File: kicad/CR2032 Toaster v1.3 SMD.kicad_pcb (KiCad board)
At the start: 2 copper layers, 26 x 16.5 mm, 8 parts, among them J1 Conn_01x01, J2 Conn_01x01

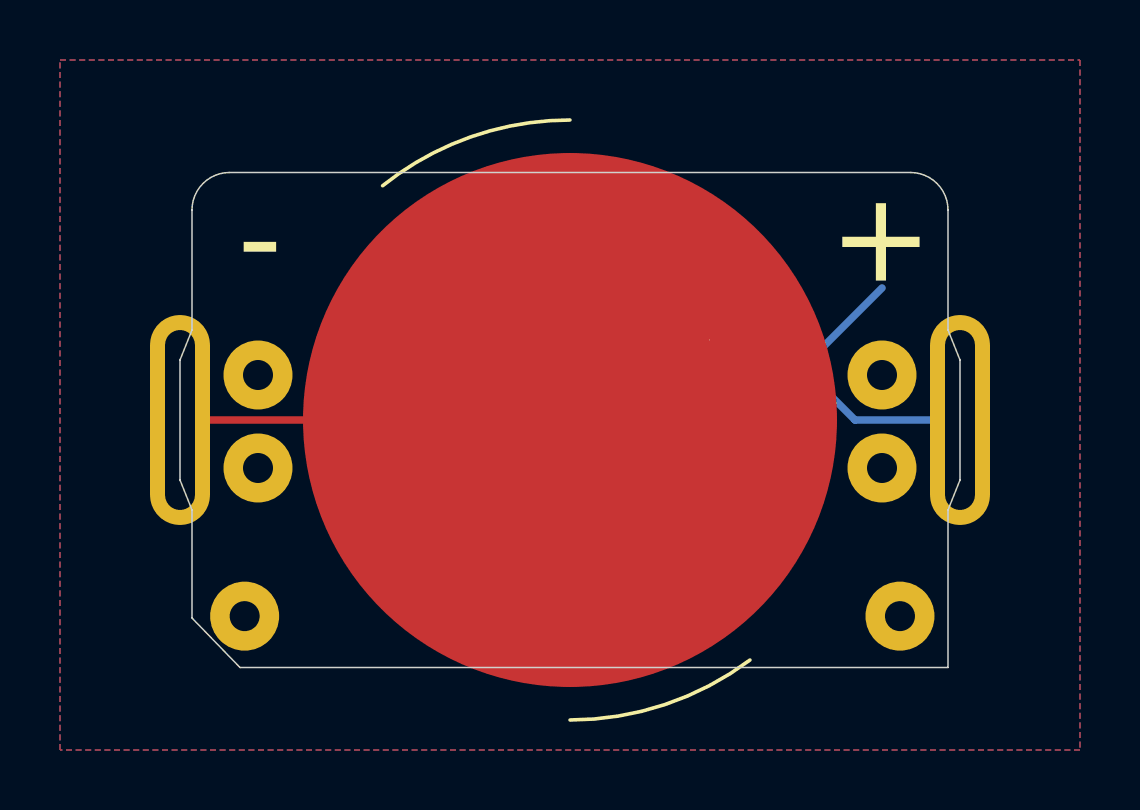
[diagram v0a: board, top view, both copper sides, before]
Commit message: Changed footprint to SMD and adjusted pad sizes
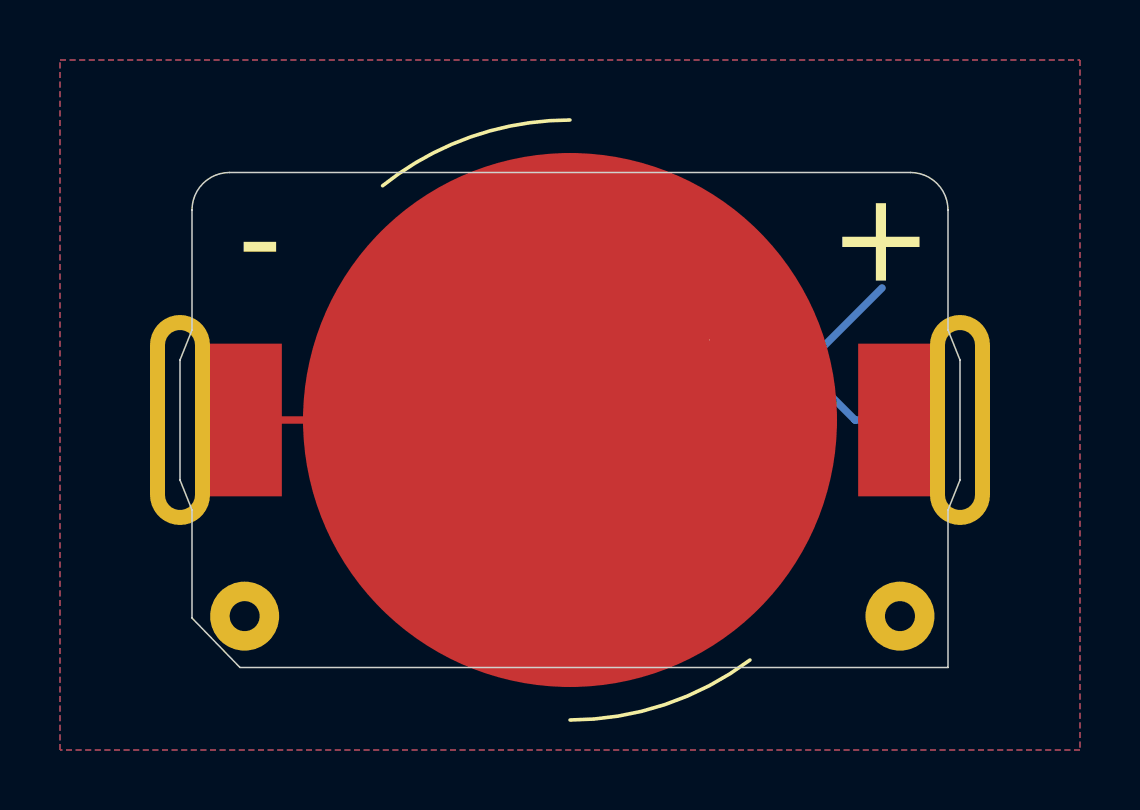
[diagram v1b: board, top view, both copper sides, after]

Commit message: Modified 1.3 for SMD, with Gerber File
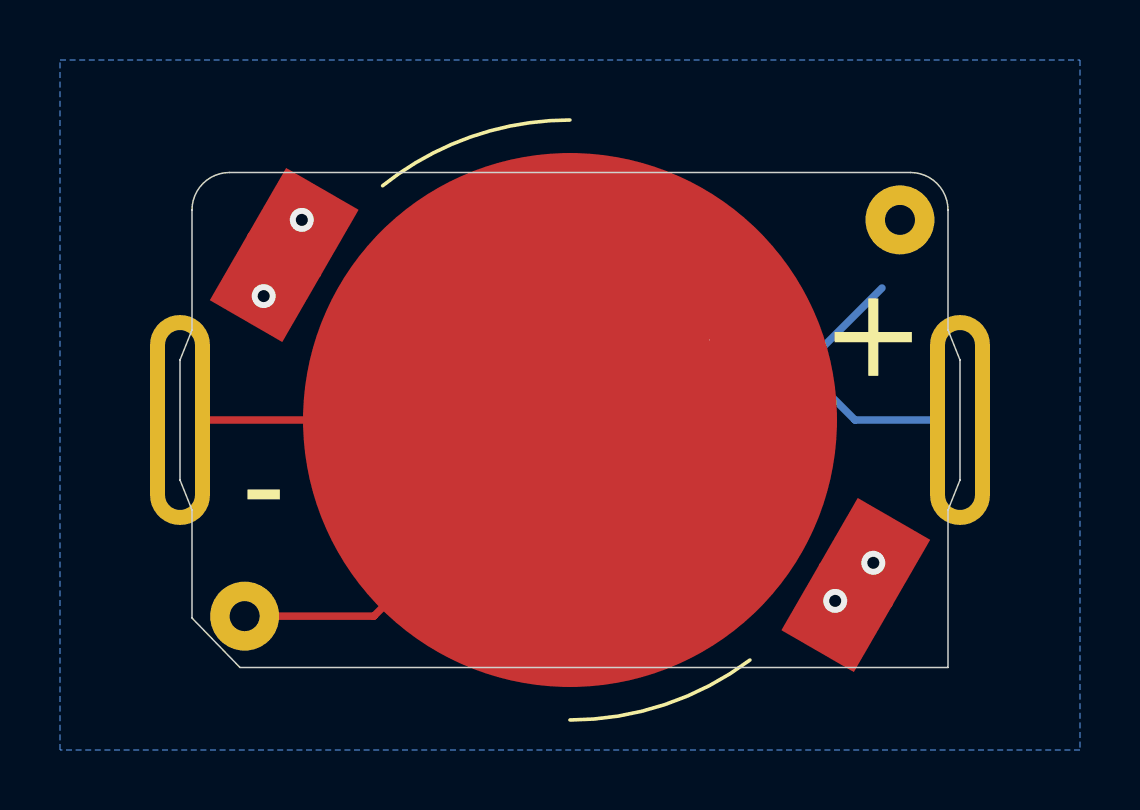
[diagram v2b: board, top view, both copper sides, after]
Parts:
- BT1: value BAT-HLD-001-THM -> BLK-912
- moved REF** 13.2 mm to (119.0, 100.3)
- turned BT1 to 330 degrees
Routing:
- net Net-(BT1-PadN): track 16.2 -> 29.8 mm
- net Net-(BT1-PadP1): vias 0 -> 4
- removed copper zone on F.Cu, net Net-(BT1-PadN)
